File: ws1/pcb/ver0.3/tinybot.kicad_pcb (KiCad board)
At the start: 2 copper layers, 41.3 x 44.5 mm, 20 parts, among them IC1 ATTINY84-P, P1 PWR, P2 Pin Breakout, P3 ICSP, P4 M1, P5 M2, U1 LD1117S33TR, U2 L293D

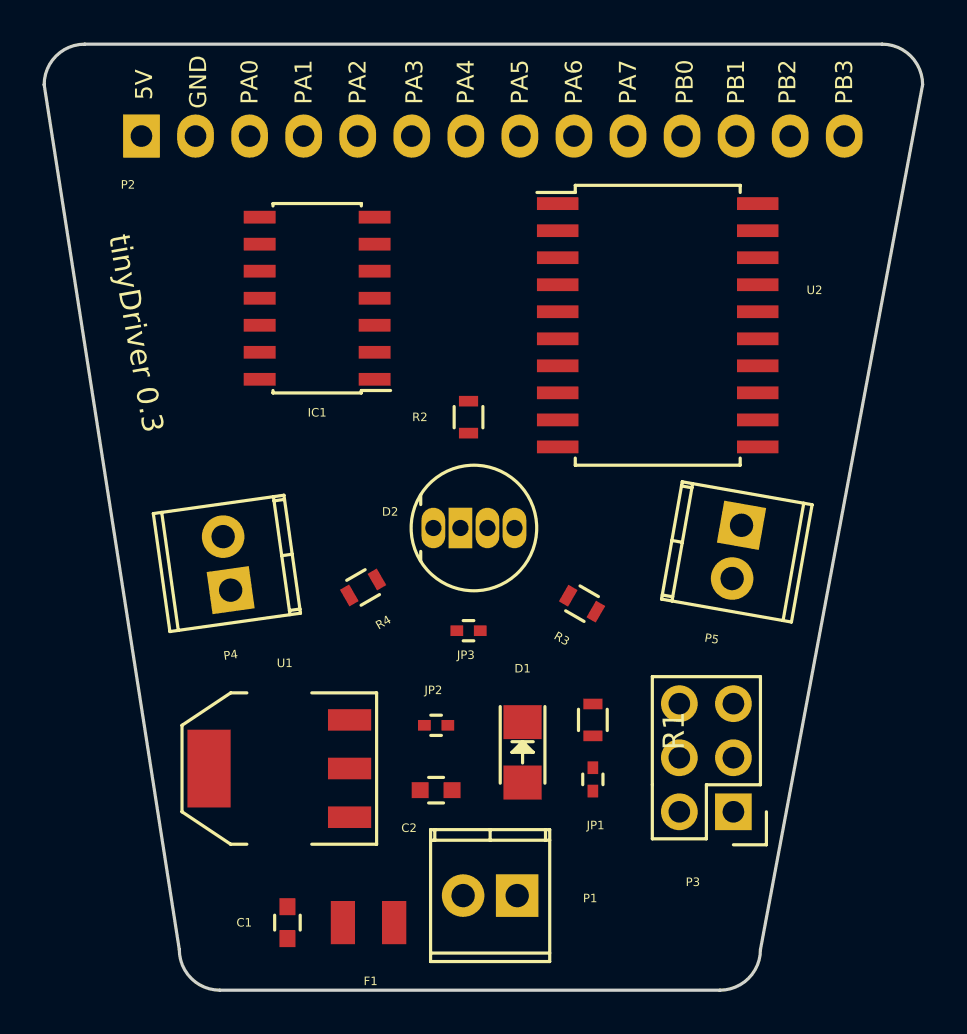
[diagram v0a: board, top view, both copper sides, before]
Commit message: switching to DRV8835 and qfn
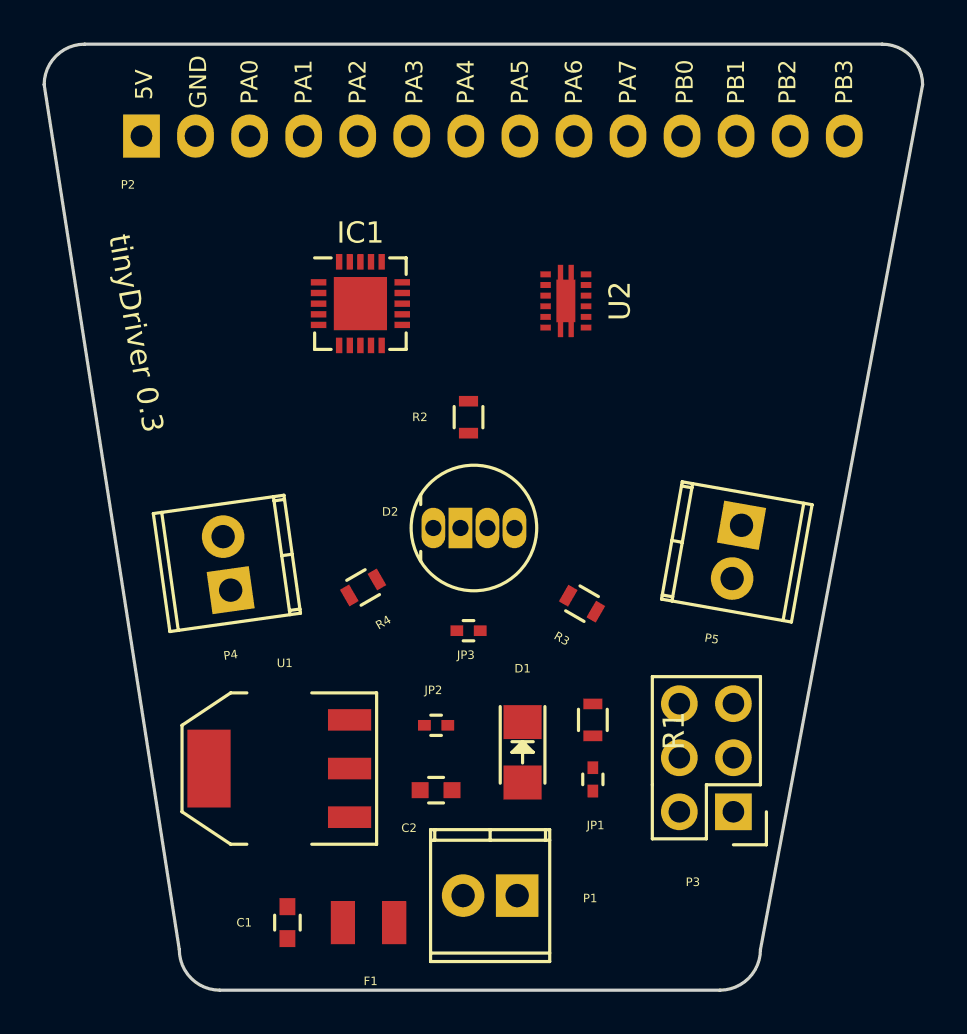
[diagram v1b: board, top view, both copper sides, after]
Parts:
- IC1: value ATTINY84-P -> ATTINY84-M; footprint Housings_SOIC:SOIC-14_3.9x8.7mm_Pitch1.27mm -> Housings_DFN_QFN:QFN-20-1EP_4x4mm_Pitch0.5mm
- U2: value L293D -> DRV8835; footprint Housings_SOIC:SOIC-20_7.5x12.8mm_Pitch1.27mm -> tinybot:DRV8835
- moved U2 4.47 mm to (147.1, 76.8), turned to 90 degrees
- moved IC1 2.05 mm to (137.4, 77.0), turned to 0 degrees
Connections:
- IC1 pad 1: VCC -> PH2
- IC1 pad 10: DIR1A -> (no net)
- IC1 pad 13: Net-(IC1-Pad13) -> RESET
- IC1 pad 14: GND -> Net-(IC1-Pad14)
- IC1 pad 2: DIR2A -> PH1
- IC1 pad 3: DIR2B -> Net-(IC1-Pad3)
- IC1 pad 4: RESET -> Net-(IC1-Pad4)
- IC1 pad 6: Net-(IC1-Pad6) -> (no net)
- IC1 pad 7: MOSI -> (no net)
- IC1 pad 8: MISO -> GND
- IC1 pad 9: DIR1B -> VCC
- JP2 pad 1: VIN -> VCC
- P2 pad 10: Net-(IC1-Pad6) -> MODE
- P2 pad 11: DIR2A -> Net-(IC1-Pad11)
- P2 pad 12: DIR2B -> Net-(IC1-Pad12)
- P2 pad 13: Net-(IC1-Pad5) -> Net-(IC1-Pad14)
- P2 pad 3: Net-(IC1-Pad13) -> Net-(IC1-Pad5)
- P2 pad 4: Net-(IC1-Pad12) -> Net-(IC1-Pad4)
- P2 pad 5: Net-(IC1-Pad11) -> Net-(IC1-Pad3)
- P2 pad 6: DIR1A -> PH1
- P2 pad 7: DIR1B -> PH2
- P3 pad 3: DIR1B -> PH2
- R2 pad 2: Net-(IC1-Pad12) -> Net-(IC1-Pad4)
- R3 pad 2: Net-(IC1-Pad13) -> Net-(IC1-Pad5)
- R4 pad 2: Net-(IC1-Pad11) -> Net-(IC1-Pad3)
- U2 pad 1: MOSI -> VIN
- U2 pad 10: DIR2A -> PH1
- U2 pad 11: Net-(P5-Pad2) -> MODE
- U2 pad 12: GND -> Net-(JP2-Pad2)
- U2 pad 2: DIR1A -> Net-(P4-Pad1)
- U2 pad 4: GND -> Net-(P5-Pad1)
- U2 pad 5: GND -> Net-(P5-Pad2)
- U2 pad 6: Net-(P4-Pad1) -> GND
- U2 pad 7: DIR1B -> MISO
- U2 pad 8: Net-(JP2-Pad2) -> PH2
- U2 pad 9: MISO -> MOSI

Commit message: added mosfet
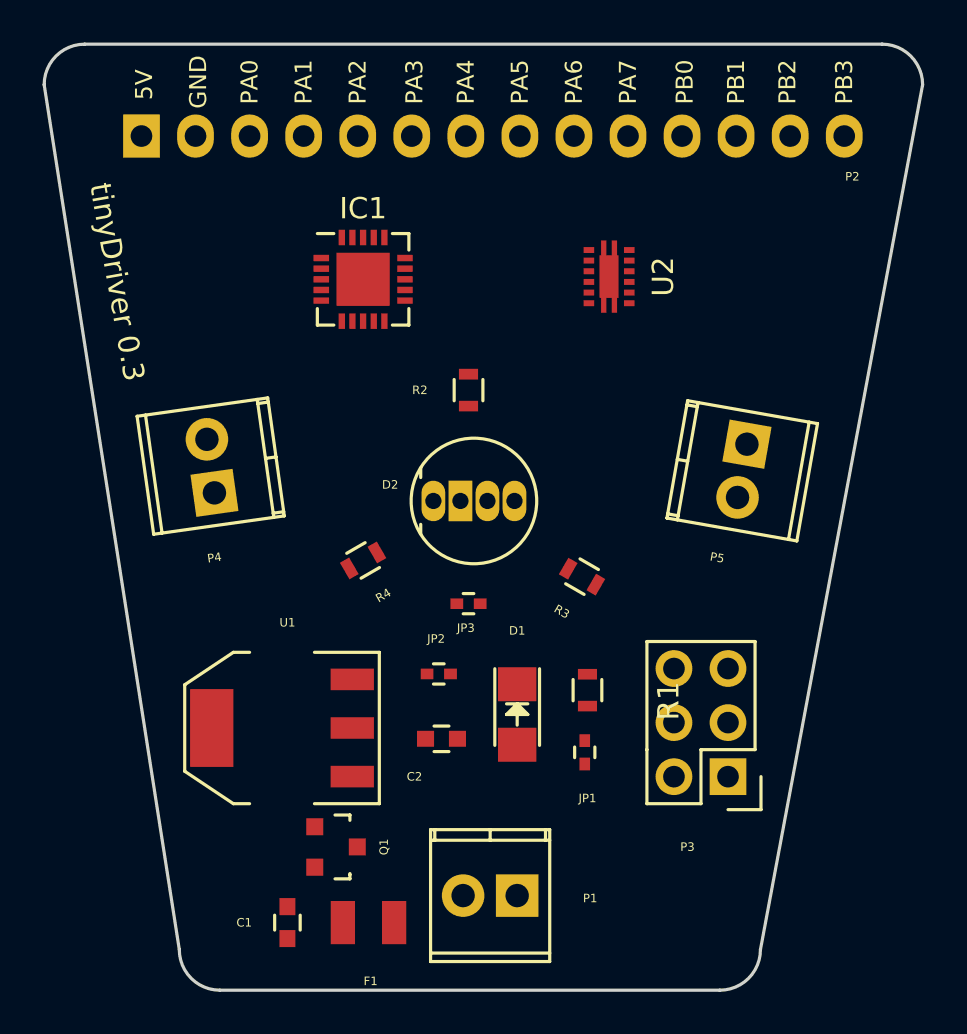
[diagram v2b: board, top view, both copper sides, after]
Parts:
- added Q1: NCE3407A, TO_SOT_Packages_SMD:SOT-23, F.Cu at (136.3, 102.5)
- moved P4 4.64 mm to (130.6, 85.9)
- moved P5 3.82 mm to (155.6, 83.6)
- moved C2 2.43 mm to (141.2, 97.4)
- moved JP2 2.42 mm to (141.1, 94.4)
- moved U2 2.33 mm to (149.1, 75.7)
- moved U1 1.91 mm to (133.7, 96.9)
- moved D1 1.80 mm to (144.8, 96.3)
- moved P3 1.67 mm to (154.7, 99.2)
- moved R1 1.42 mm to (148.1, 95.1)
- moved JP1 1.33 mm to (148.0, 98.0)
- moved R2 1.27 mm to (142.5, 81.0)
- moved D2 1.27 mm to (140.8, 86.2)
- moved JP3 1.27 mm to (142.5, 91.1)
- moved R3 1.27 mm to (147.8, 89.8)
- moved R4 1.27 mm to (137.5, 89.0)
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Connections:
- F1 pad 2: Net-(C1-Pad1) -> Net-(F1-Pad2)
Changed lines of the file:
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@@
 (kicad_pcb (version 4) (host pcbnew 4.0.1-stable)
   (general
-    (links 54)
-    (no_connects 54)
+    (links 56)
+    (no_connects 56)
     (area 122.479999 64.694999 163.905001 109.295001)
     (thickness 1.6)
@@
     (tracks 0)
     (zones 0)
-    (modules 20)
-    (nets 28)
+    (modules 21)
+    (nets 29)
   )
   (page A4)
@@
   (net 26 "Net-(IC1-Pad4)")
   (net 27 "Net-(IC1-Pad14)")
+  (net 28 "Net-(F1-Pad2)")
   (net_class Default "This is the default net class."
     (clearance 0.2)
@@
     (add_net "Net-(D2-Pad3)")
     (add_net "Net-(D2-Pad4)")
+    (add_net "Net-(F1-Pad2)")
     (add_net "Net-(IC1-Pad11)")
     (add_net "Net-(IC1-Pad12)")
@@
   )
   (module Capacitors_SMD:C_0402 (layer F.Cu)
-    (at 148.336 99.314 270)
+    (at 147.955 98.044 270)
     (descr "Capacitor SMD 0402, reflow soldering, AVX (see smccp.pdf)")
     (tags "capacitor 0402")
@@
   )
   (module Pin_Headers:Pin_Header_Straight_2x03 (layer F.Cu)
-    (at 154.94 100.838 180)
+    (at 154.686 99.187 180)
     (descr "Through hole pin header")
     (tags "pin header")
@@
   )
   (module Capacitors_SMD:C_0603 (layer F.Cu)
-    (at 140.97 99.822)
+    (at 141.224 97.409)
     (descr "Capacitor SMD 0603, reflow soldering, AVX (see smccp.pdf)")
     (tags "capacitor 0603")
@@
   )
   (module LEDs:LED_1206 (layer F.Cu)
-    (at 145.034 98.044 270)
+    (at 144.78 96.266 270)
     (descr "LED 1206 smd package")
     (tags "LED1206 SMD")
@@
   )
   (module Resistors_SMD:R_0603 (layer F.Cu)
-    (at 148.336 96.52 270)
+    (at 148.082 95.123 270)
     (descr "Resistor SMD 0603, reflow soldering, Vishay (see dcrcw.pdf)")
     (tags "resistor 0603")
@@
   )
   (module Resistors_SMD:R_0603 (layer F.Cu)
-    (at 142.494 82.296 90)
+    (at 142.494 81.026 90)
     (descr "Resistor SMD 0603, reflow soldering, Vishay (see dcrcw.pdf)")
     (tags "resistor 0603")
@@
   )
   (module Resistors_SMD:R_0603 (layer F.Cu)
-    (at 147.828 91.059 150)
+    (at 147.828 89.789 150)
     (descr "Resistor SMD 0603, reflow soldering, Vishay (see dcrcw.pdf)")
     (tags "resistor 0603")
@@
   )
   (module tinybot:SOT-223 (layer F.Cu)
-    (at 133.604 98.806 90)
+    (at 133.731 96.901 90)
     (descr "module CMS SOT223 4 pins")
     (tags "CMS SOT")
@@
   )
   (module Terminal_Blocks:TerminalBlock_Pheonix_MPT-2.54mm_2pol (layer F.Cu)
-    (at 131.318 90.424 98)
+    (at 130.556 85.852 98)
     (descr "2-way 2.54mm pitch terminal block, Phoenix MPT series")
     (fp_text reference P4 (at -3.018337 -0.4242 368) (layer F.SilkS)
@@
   )
   (module Terminal_Blocks:TerminalBlock_Pheonix_MPT-2.54mm_2pol (layer F.Cu)
-    (at 155.321 87.376 260)
+    (at 155.575 83.566 260)
     (descr "2-way 2.54mm pitch terminal block, Phoenix MPT series")
     (fp_text reference P5 (at 5.495551 0.449537 350) (layer F.SilkS)
@@
   )
   (module LEDs:LED-RGB-5MM_Common_Cathode (layer F.Cu)
-    (at 140.843 87.503 90)
+    (at 140.843 86.233 90)
     (descr "5mm common cathode RGB LED")
     (tags "RGB LED 5mm Common Cathode")
@@
       (net 1 VIN))
     (pad 2 smd rect (at 1.20396 0 270) (size 2.02946 1.14046) (layers F.Cu F.Paste F.Mask)
-      (net 17 "Net-(C1-Pad1)"))
+      (net 28 "Net-(F1-Pad2)"))
   )
   (module Resistors_SMD:R_0603 (layer F.Cu)
-    (at 137.541 90.297 210)
+    (at 137.541 89.027 210)
     (descr "Resistor SMD 0603, reflow soldering, Vishay (see dcrcw.pdf)")
     (tags "resistor 0603")
@@
   )
   (module Capacitors_SMD:C_0402 (layer F.Cu)
-    (at 140.97 96.774 180)
+    (at 141.097 94.361 180)
     (descr "Capacitor SMD 0402, reflow soldering, AVX (see smccp.pdf)")
     (tags "capacitor 0402")
@@
   )
   (module Capacitors_SMD:C_0402 (layer F.Cu)
-    (at 142.494 92.329)
+    (at 142.494 91.059)
     (descr "Capacitor SMD 0402, reflow soldering, AVX (see smccp.pdf)")
     (tags "capacitor 0402")
@@
     (descr "Through hole pin header")
     (tags "pin header")
-    (fp_text reference P2 (at -2.286 -0.635 180) (layer F.SilkS)
+    (fp_text reference P2 (at -1.905 33.401 180) (layer F.SilkS)
       (effects (font (size 0.4 0.4) (thickness 0.08)))
     )
@@
   )
   (module tinybot:DRV8835 (layer F.Cu)
-    (at 147.066 76.835 90)
+    (at 149.098 75.692 90)
     (fp_text reference U2 (at 0 2.54 90) (layer F.SilkS)
       (effects (font (size 1 1) (thickness 0.15)))
     )
-    (fp_text value DRV8835 (at 0 -2.54 90) (layer F.Fab)
+    (fp_text value DRV8835 (at 0 -2.54 90) (layer F.Fab) hide
       (effects (font (size 1 1) (thickness 0.15)))
     )
@@
   )
   (module Housings_DFN_QFN:QFN-20-1EP_4x4mm_Pitch0.5mm (layer F.Cu)
-    (at 137.414 76.962)
+    (at 137.541 75.819)
     (descr "20-Lead Plastic Quad Flat, No Lead Package (ML) - 4x4x0.9 mm Body [QFN]; (see Microchip Packaging Specification 00000049BS.pdf)")
     (tags "QFN 0.5")
@@
       (effects (font (size 1 1) (thickness 0.15)))
     )
-    (fp_text value ATTINY84-M (at 0 3.33) (layer F.Fab)
+    (fp_text value ATTINY84-M (at 0 3.33) (layer F.Fab) hide
       (effects (font (size 1 1) (thickness 0.15)))
     )
@@
     )
   )
+  (module TO_SOT_Packages_SMD:SOT-23 (layer F.Cu)
+    (at 136.271 102.489 270)
+    (descr "SOT-23, Standard")
+    (tags SOT-23)
+    (attr smd)
+    (fp_text reference Q1 (at 0 -2.25 270) (layer F.SilkS)
+      (effects (font (size 0.4 0.4) (thickness 0.08)))
+    )
+    (fp_text value NCE3407A (at 0 2.3 270) (layer F.Fab) hide
+      (effects (font (size 1 1) (thickness 0.15)))
+    )
+    (fp_line (start -1.65 -1.6) (end 1.65 -1.6) (layer F.CrtYd) (width 0.05))
+    (fp_line (start 1.65 -1.6) (end 1.65 1.6) (layer F.CrtYd) (width 0.05))
+    (fp_line (start 1.65 1.6) (end -1.65 1.6) (layer F.CrtYd) (width 0.05))
+    (fp_line (start -1.65 1.6) (end -1.65 -1.6) (layer F.CrtYd) (width 0.05))
+    (fp_line (start 1.29916 -0.65024) (end 1.2509 -0.65024) (layer F.SilkS) (width 0.15))
+    (fp_line (start -1.49982 0.0508) (end -1.49982 -0.65024) (layer F.SilkS) (width 0.15))
+    (fp_line (start -1.49982 -0.65024) (end -1.2509 -0.65024) (layer F.SilkS) (width 0.15))
+    (fp_line (start 1.29916 -0.65024) (end 1.49982 -0.65024) (layer F.SilkS) (width 0.15))
+    (fp_line (start 1.49982 -0.65024) (end 1.49982 0.0508) (layer F.SilkS) (width 0.15))
+    (pad 1 smd rect (at -0.95 1.00076 270) (size 0.8001 0.8001) (layers F.Cu F.Paste F.Mask)
+      (net 2 GND))
+    (pad 2 smd rect (at 0.95 1.00076 270) (size 0.8001 0.8001) (layers F.Cu F.Paste F.Mask)
+      (net 17 "Net-(C1-Pad1)"))
+    (pad 3 smd rect (at 0 -0.99822 270) (size 0.8001 0.8001) (layers F.Cu F.Paste F.Mask)
+      (net 28 "Net-(F1-Pad2)"))
+    (model TO_SOT_Packages_SMD.3dshapes/SOT-23.wrl
+      (at (xyz 0 0 0))
+      (scale (xyz 1 1 1))
+      (rotate (xyz 0 0 0))
+    )
+  )
   (gr_text GND (at 129.794 66.548 90) (layer F.SilkS)
     (effects (font (size 0.8 0.8) (thickness 0.15)))
   )
-  (gr_text "tinyDriver 0.3" (at 126.873 78.359 280) (layer F.SilkS)
+  (gr_text "tinyDriver 0.3" (at 125.984 75.946 280) (layer F.SilkS)
     (effects (font (size 1 1) (thickness 0.2)))
   )

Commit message: updated schematic and pcb added mounting holes
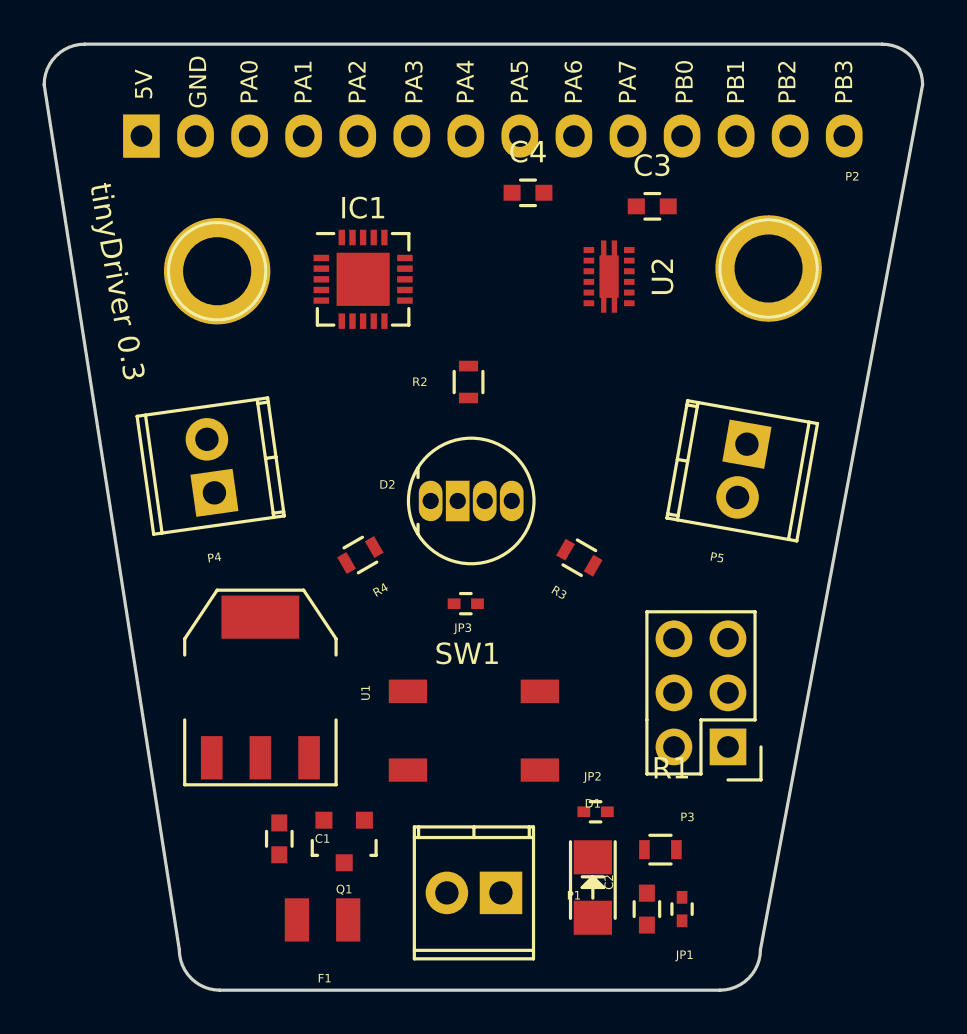
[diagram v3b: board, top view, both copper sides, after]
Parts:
- added C3: 0.1uF, Capacitors_SMD:C_0603, F.Cu at (151.1, 72.4)
- added C4: 10uF, Capacitors_SMD:C_0603, F.Cu at (145.3, 71.8)
- added REF**: 1pin, tinybot:1pin, F.Cu at (156.6, 75.3)
- added REF**: 1pin, tinybot:1pin, F.Cu at (130.7, 75.4)
- added SW1: SW_PUSH, tinybot:SWITCH_SKQGAKE010, F.Cu at (142.7, 97.0)
- moved C2 12.5 mm to (150.9, 105.4), turned to 270 degrees
- moved JP2 9.81 mm to (148.5, 100.8)
- moved D1 8.87 mm to (148.3, 104.4)
- moved JP1 8.67 mm to (152.5, 105.4)
- moved R1 8.24 mm to (151.5, 102.6), turned to 0 degrees
- moved C1 3.96 mm to (133.6, 102.1), turned to 270 degrees
- moved F1 2.16 mm to (135.6, 105.9)
- moved U1 2.16 mm to (132.7, 95.0), turned to 0 degrees
- moved P3 1.40 mm to (154.7, 97.8)
- moved R3 0.90 mm to (147.7, 88.9)
- moved P1 0.77 mm to (144.0, 104.6)
- moved Q1 0.46 mm to (136.7, 102.2), turned to 180 degrees
- moved R2 0.38 mm to (142.5, 80.6)
- moved R4 0.28 mm to (137.4, 88.8)
- moved JP3 0.13 mm to (142.4, 91.1)
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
